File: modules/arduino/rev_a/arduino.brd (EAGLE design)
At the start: 67.3 x 66.7 mm, 58 parts, among them J1 MODULE_GENERIC, J3 ICSP_PROG, J4 MICRO_USB_B_HIROSE_ZX62-B-5PA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, J6 ICSP, U1 ADG3304, U2 ADG3304, U3 ATMEGA8U2-MU, U4 ATMEGA328P-20MU, U5 74LVC2G00DC, U6 SN74LVC1G123DCUR, Y1 12 MHz, Y2 16MHz

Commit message: Seinduino routed
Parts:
- removed RN2, RN3: 1K, resistor-dil:CAY16
- added C16: 100nF, passives:0603_CAP
- added R10, R11, R12, R7, R8: 1kΩ, passives:0603-RES
- added R9: 470Ω, passives:0603-RES
- C4, C6: value 100n -> 100nF; device SmartPrj:C0603-ROUND -> passives:0603_CAP
- C7: device SmartPrj:C0603-ROUND -> passives:0603_CAP
- U1: value ADG3304 -> ATMEGA8U2-MU; device chips:TSSOP-14/5MM -> atmel:QFN32
- U2: value ADG3304 -> ATMEGA328P-20MU; device chips:TSSOP-14/5MM -> idii:MLF32
- U3: value ATMEGA8U2-MU -> ADG3304; device atmel:QFN32 -> chips:TSSOP-14/5MM
- U4: value ATMEGA328P-20MU -> ADG3304; device idii:MLF32 -> chips:TSSOP-14/5MM
- moved R6 93.4 mm to (33.8, 42.2), turned to 270 degrees
- moved C14 89.4 mm to (43.7, 19.6)
- moved RN1 85.1 mm to (47.8, 13.5), turned to 90 degrees
- moved C15 83.1 mm to (41.1, 9.78), turned to 180 degrees
- moved C5 82.7 mm to (47.8, 17.3), turned to 180 degrees
- moved U5 70.4 mm to (42.2, 13.0), turned to 180 degrees
- moved U6 63.8 mm to (42.2, 16.5), turned to 270 degrees
- moved RESET-SIGN-EN 52.3 mm to (36.8, 16.3), turned to 90 degrees
- moved U3 36.9 mm to (57.7, 27.2), turned to 0 degrees
- moved C1 24.1 mm to (59.9, 31.8), turned to 180 degrees
- moved C3 23.5 mm to (26.2, 37.7)
- moved ON 22.2 mm to (41.1, 22.9), turned to 90 degrees
- moved U4 20.6 mm to (28.2, 42.2), turned to 180 degrees
- moved C13 20.2 mm to (33.8, 39.1), turned to 90 degrees
- moved L 20.0 mm to (36.6, 22.9), turned to 90 degrees
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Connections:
- removed net N$10: RESET-SIGN-EN.2, RN1.7, U5.2
- removed net N$9: RESET-PROG-EN.2, RN1.8, U5.1
- net +5V: now also R7.2, R8.2, R9.1, U3.14, U4.14; no longer RN2.2, RN2.3, RN3.3, RN3.4, U1.14, U2.14
- net AD0: now also U2.23; no longer U4.23
- net AD1: now also U2.24; no longer U4.24
- net AD2: now also U2.25; no longer U4.25
- net AD3: now also U2.26; no longer U4.26
- net AD4: now also U2.27; no longer U4.27
- net AD5: now also U2.28; no longer U4.28
- net ARD_USB_D+_TERM: now also U1.29; no longer U3.29
- net ARD_USB_D-_TERM: now also U1.30; no longer U3.30
- net ARD_USB_GND: now also U1.28; no longer U3.28
- net AREF: now also U2.20; no longer U4.20
- net DTR_PROG: now also RESET-PROG-EN.2, RN1.8, U1.13, U5.1; no longer U3.13
- net GND: now also C16.2, C6.2, RN1.5, U1.3, U1.EXP, U2.21, U2.3, U2.5, U3.7, U4.7; no longer C6.1, RN1.6, U1.7, U2.7, U3.3, U3.EXP, U4.21, U4.3, U4.5
- net IO0: now also R11.2, U2.30; no longer RN3.2, U4.30
- net IO1: now also R12.2, U2.31; no longer RN3.1, U4.31
- net IO2: now also U2.32; no longer U4.32
- net IO3: now also U2.1; no longer U4.1
- net IO4: now also U2.2; no longer U4.2
- net IO5: now also U2.9; no longer U4.9
- net IO6: now also U2.10; no longer U4.10
- net IO7: now also U2.11; no longer U4.11
- net IO8: now also U2.12; no longer U4.12
- net IO9: now also U2.13; no longer U4.13
- net M8RXD: now also R11.1, U1.9; no longer RN3.7, U3.9
- net M8TXD: now also R12.1, U1.8; no longer RN3.8, U3.8
- net MISO: now also U2.16, U3.2; no longer U2.2, U4.16
- net MISO_PROG: now also U1.17, U4.4; no longer U1.2, U3.17
- net MISO_PROG_SHIFTED: now also U4.11; no longer U1.13
- net MISO_SHIFTED: now also U3.13; no longer U2.13
- net MOD_IN: now also RESET-SIGN-EN.2, RN1.7, U5.2
- net MOSI: now also U2.15, U3.3; no longer U2.3, U4.15
- net MOSI_PROG: now also U1.16, U4.3; no longer U1.3, U3.16
- net MOSI_PROG_SHIFTED: now also U4.12; no longer U1.12
- net MOSI_SHIFTED: now also U3.12; no longer U2.12
- net N$1: now also R10.2; no longer RN2.1
- net N$2: now also U1.18; no longer U3.18
- net N$3: now also R9.2; no longer RN3.5, RN3.6
- net N$35: now also R8.1; no longer RN2.7
- net N$36: now also R7.1; no longer RN2.6
- net N$4: now also U1.19; no longer U3.19
- net N$5: now also U1.20; no longer U3.20
- net N$6: now also U1.21; no longer U3.21
- net N$7: now also RN1.4; no longer RN1.3
- net RESET: now also RN1.6, U2.29, U3.5; no longer RN1.5, U2.5, U4.29
- net RESET_PROG: now also U1.24, U4.5; no longer U1.5, U3.24
- net RESET_PROG_SHIFTED: now also U4.10; no longer U1.10
- net RESET_SHIFTED: now also U3.10; no longer U2.10
- net RXLED: now also U1.10; no longer U3.10
- net SCK: now also R10.1, U2.17, U3.4; no longer RN2.8, U2.4, U4.17
- net SCK_PROG: now also U1.15, U4.2; no longer U1.4, U3.15
- net SCK_PROG_SHIFTED: now also U4.13; no longer U1.11
- net SCK_SHIFTED: now also U3.11; no longer U2.11
- net SS: now also U2.14; no longer U4.14
- net TXLED: now also U1.11; no longer U3.11
- net USBVCC: now also U1.31; no longer U3.31
- net VCC: now also C16.1, C6.1, RN1.3, U1.32, U1.4, U2.18, U2.4, U2.6, U3.1, U3.8, U4.1, U4.8; no longer C6.2, RN1.4, U1.1, U1.8, U2.1, U2.8, U3.32, U3.4, U4.18, U4.4, U4.6
- net VUCAP: now also U1.27; no longer U3.27
- net XT1: now also U1.1; no longer U3.1
- net XT2: now also U1.2; no longer U3.2
- net XTAL1: now also U2.7; no longer U4.7
- net XTAL2: now also U2.8; no longer U4.8
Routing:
- net VCC: track 21.3 -> 190.9 mm, vias 0 -> 9
- net +5V: track 33.5 -> 127.4 mm, vias 0 -> 6
- net AD5: track 0.63 -> 91.1 mm, vias 0 -> 4
- net AD4: track 0.00 -> 87.6 mm, vias 0 -> 4
- net RESET: track 0.00 -> 69.5 mm, vias 0 -> 3
- net SCK: track 6.45 -> 59.1 mm, vias 1 -> 3
- net M8TXD: track 0.00 -> 50.7 mm, vias 0 -> 2
- net M8RXD: track 0.00 -> 49.6 mm, vias 0 -> 2
- net MISO: track 0.00 -> 45.2 mm, vias 0 -> 2
- net DTR_PROG: track 0.00 -> 45.2 mm, vias 0 -> 4
- net MOSI: track 0.00 -> 43.7 mm, vias 0 -> 2
- net MOD_IN: track 7.02 -> 48.8 mm, vias 1 -> 7
- net AREF: track 12.5 -> 49.6 mm
- net AD3: track 0.00 -> 33.7 mm
- net AD2: track 0.00 -> 31.9 mm
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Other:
- board text added: "Note: Pad connects to ground, but this part from Arduino neglects that, and they do not provide lbrs so cannot fix :("
- board text removed: "L"

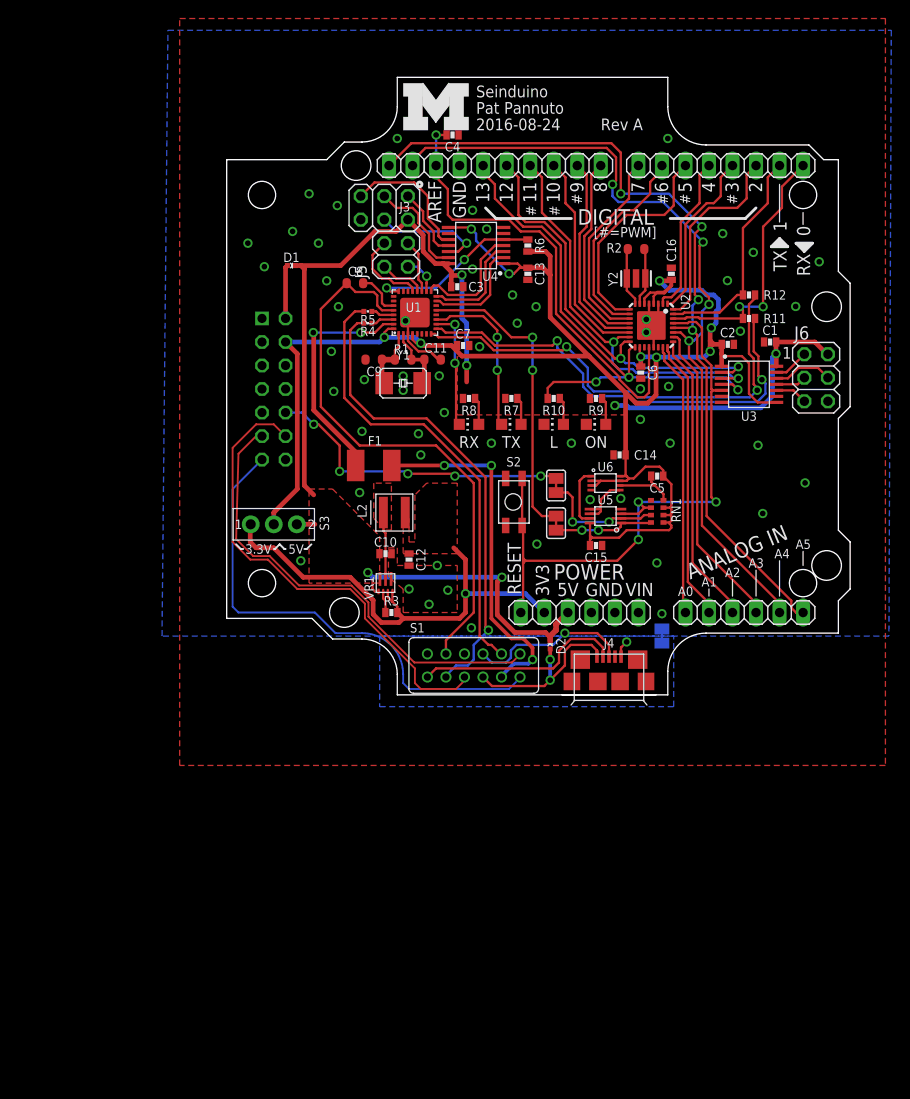
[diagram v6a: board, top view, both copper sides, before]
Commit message: Seinduino: Curve USB, tighten up dimension layer
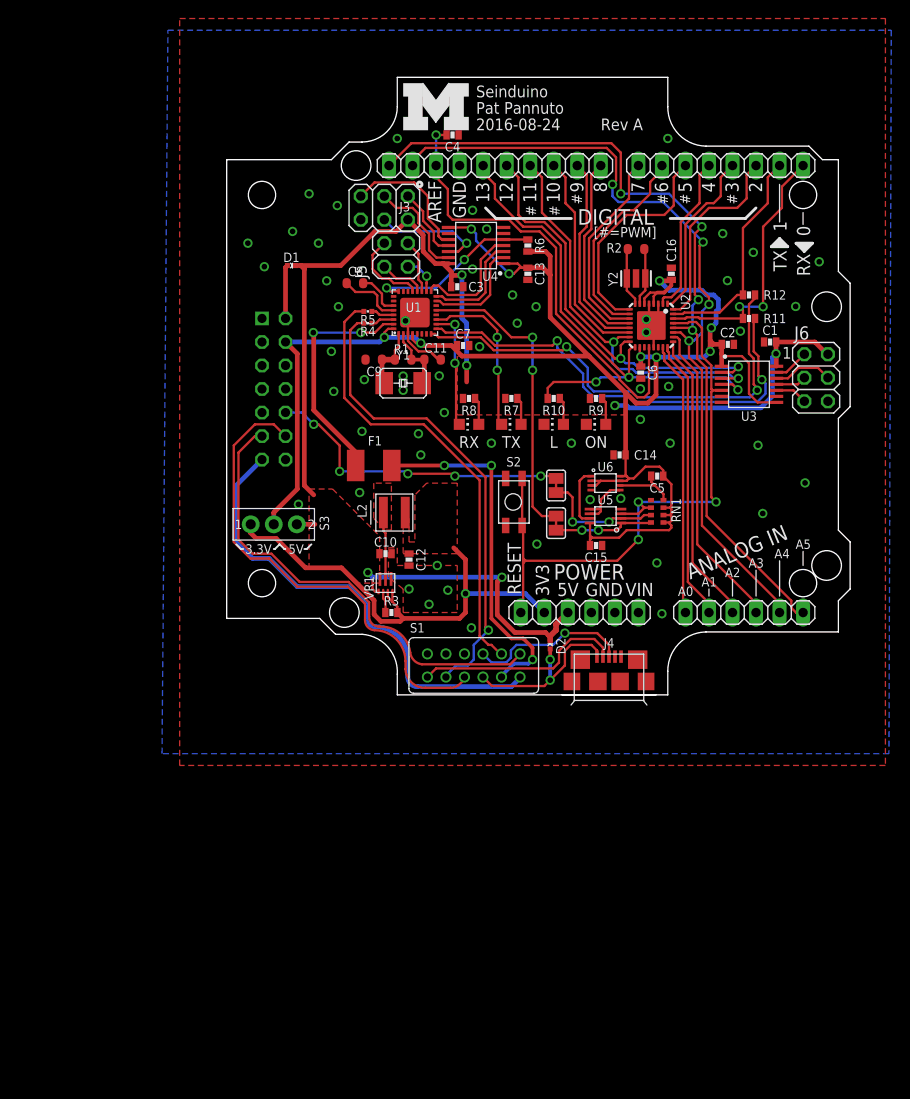
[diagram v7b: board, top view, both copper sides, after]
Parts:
- removed GROUND: (no value), jumper:SJ
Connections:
- removed net ARD_USB_GND: C8.2, S1.11, U1.28
- removed net EXT_USB_GND: GROUND.1, J4.5, S1.12
- net GND: now also C8.2, J4.5, S1.11, S1.12, U1.28; no longer GROUND.2
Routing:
- net ARD_USB_GND: track 61.0 -> 0.00 mm
- net GND: track 17.2 -> 22.7 mm
- net MOD_USB_VBUS: track 53.1 -> 49.7 mm
- net EXT_USB_GND: track 1.84 -> 0.00 mm, vias 1 -> 0
- net MOD_USB_D-: track 51.7 -> 50.9 mm
- net +3V3: track 51.7 -> 51.0 mm
- removed copper zone on layer 16, net EXT_USB_GND
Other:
- outline, holes or cut-outs redrawn

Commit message: seinduino: renumber / normalize components
 - Change 1MΩ resistors to all use same package
 - Renumber caps
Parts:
- C1, C2: value 100nF -> 22pF; device passives:0603_CAP -> SmartPrj:C0603-ROUND
- C10: value 10uF -> 100nF
- C11, C9: value 22p -> 100nF; device SmartPrj:C0603-ROUND -> passives:0603_CAP
- C12: value 22uF -> 100nF
- C14: value 100nF -> 1uF; device passives:0603_CAP -> SmartPrj:C0603-ROUND
- C15: value 100nF -> 10uF
- C16: value 100nF -> 22uF
- C8: value 1uF -> 100nF; device SmartPrj:C0603-ROUND -> passives:0603_CAP
- R1, R2: value 1M -> 1MΩ; device SmartPrj:R0603-ROUND -> passives:0603-RES
- moved C1 42.8 mm to (17.1, 29.8)
- moved C16 41.9 mm to (21.0, 8.26), turned to 270 degrees
- moved C8 40.8 mm to (55.4, 31.5)
- moved C14 34.1 mm to (15.1, 38.1), turned to 180 degrees
- moved C10 33.9 mm to (33.8, 39.1), turned to 90 degrees
- moved C7 33.1 mm to (59.9, 31.8), turned to 180 degrees
- moved C4 32.7 mm to (46.0, 28.4), turned to 270 degrees
- moved C6 32.7 mm to (25.7, 54.1), turned to 180 degrees
- moved C2 31.9 mm to (23.5, 29.8), turned to 0 degrees
- moved C13 30.2 mm to (41.1, 9.78), turned to 180 degrees
- moved C12 28.3 mm to (47.8, 17.3), turned to 180 degrees
- moved C15 22.8 mm to (18.4, 8.89), turned to 0 degrees
- moved C11 22.7 mm to (43.7, 19.6)
- moved C5 21.9 mm to (49.3, 39.1), turned to 90 degrees
- moved C9 12.0 mm to (26.2, 37.7), turned to 0 degrees
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- renumbered AD to J-ARD-AD, IOH to J-ARD-IOH, IOL to J-ARD-IOL, JP1 to J-ARD-I2C
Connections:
- net +3V3: now also C16.1; no longer C12.1
- net +5V: now also C15.1, C7.1, C9.1; no longer C1.1, C10.1, C3.1
- net AREF: now also C6.2; no longer C4.2
- net GND: now also C10.1, C11.1, C14.2, C15.2, C2.2, C4.2, C5.2, C6.1, C8.1; no longer C10.2, C11.2, C12.2, C14.1, C15.1, C2.1, C4.1, C6.2, C8.2
- net N$7: now also C12.2; no longer C5.2
- net VCC: now also C10.2, C11.2, C12.1, C3.1, C4.1, C8.2; no longer C14.2, C15.2, C16.1, C2.2, C6.1, C7.1
- net VUCAP: now also C14.1; no longer C8.1
- net XT1: now also C1.1; no longer C9.1
- net XT2: now also C2.1; no longer C11.1
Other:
- board text added: "2016-08-30"
- board text removed: "2016-08-24"
